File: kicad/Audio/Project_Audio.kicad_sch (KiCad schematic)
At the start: 9 parts, among them U1 PIC32MX170F256B, U2 Audio

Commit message: Revert to 3d98758
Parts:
- removed D1, D2: Diode, symbol ME218_BaseLib:Diode
- C1: value 10 uF -> Cap
- R1: value 100 k -> Res1
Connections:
- net GND: no longer C2.2, U1.8 (Vss)
- net at U1.14 (PGED3/5VT/RB5): now also U2. (Vol-)
- net at U1.15 (PGEC3/5VT/RB6): now also U2. (Vol-)
- net at U1.16 (5VT/RB7): now also U2. (Vol-)
- net at U1.18 (PGED2/5VT/RB9): now also U2. (Vol-)
- net at U1.21 (PGEC2/5VT/RB10): now also U2. (Vol-)
- net at U1.22 (RB11): now also U2. (Vol-)
- net at U1.23 (RB12): now also U2. (Vol-)
- net at U1.24 (RB13): now also U2. (Vol-)
- new net: C2.2, U1.8 (Vss)
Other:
- moved on the sheet: R1, U2

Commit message: Update audio kicad
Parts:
- added D? (x2): Diode, symbol ME218_BaseLib:Diode
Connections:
- net GND: now also C2.2, U1.8 (Vss)
- net PWN from main PIC32: now also D?.1 (K), D?.2 (A)
- net at C1.1, R1.2, U1.2 (RA0): now also D?.1 (K), D?.2 (A)
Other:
- moved on the sheet: R1
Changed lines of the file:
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@@
   (junction (at 69.85 85.09) (diameter 0) (color 0 0 0 0)
   )
+  (junction (at 63.5 85.09) (diameter 0) (color 0 0 0 0)
+  )
   (junction (at 85.09 111.76) (diameter 0) (color 0 0 0 0)
   )
@@
   (junction (at 151.13 127) (diameter 0) (color 0 0 0 0)
   )
+  (junction (at 44.45 85.09) (diameter 0) (color 0 0 0 0)
+  )
   (junction (at 85.09 104.14) (diameter 0) (color 0 0 0 0)
   )
@@
   (junction (at 85.09 67.31) (diameter 0) (color 0 0 0 0)
   )
+  (junction (at 85.09 74.93) (diameter 0) (color 0 0 0 0)
+  )
+  (wire (pts (xy 44.45 92.71) (xy 44.45 85.09))
+    (stroke (width 0) (type default) (color 0 0 0 0))
+  )
   (polyline (pts (xy 137.16 80.01) (xy 125.73 80.01))
     (stroke (width 0) (type default) (color 0 0 0 0))
@@
     (stroke (width 0) (type default) (color 0 0 0 0))
   )
-  (wire (pts (xy 55.88 85.09) (xy 58.42 85.09))
+  (wire (pts (xy 39.37 85.09) (xy 44.45 85.09))
     (stroke (width 0) (type default) (color 0 0 0 0))
   )
@@
     (stroke (width 0) (type default) (color 0 0 0 0))
   )
-  (wire (pts (xy 66.04 85.09) (xy 69.85 85.09))
+  (wire (pts (xy 57.15 85.09) (xy 63.5 85.09))
+    (stroke (width 0) (type default) (color 0 0 0 0))
+  )
+  (wire (pts (xy 63.5 85.09) (xy 69.85 85.09))
     (stroke (width 0) (type default) (color 0 0 0 0))
   )
@@
     (stroke (width 0) (type default) (color 0 0 0 0))
   )
+  (wire (pts (xy 49.53 92.71) (xy 44.45 92.71))
+    (stroke (width 0) (type default) (color 0 0 0 0))
+  )
   (wire (pts (xy 124.46 101.6) (xy 140.97 101.6))
     (stroke (width 0) (type default) (color 0 0 0 0))
   )
+  (wire (pts (xy 63.5 73.66) (xy 63.5 85.09))
+    (stroke (width 0) (type default) (color 0 0 0 0))
+  )
   (wire (pts (xy 124.46 91.44) (xy 140.97 91.44))
     (stroke (width 0) (type default) (color 0 0 0 0))
@@
     (stroke (width 0) (type default) (color 0 0 0 0))
   )
+  (wire (pts (xy 63.5 92.71) (xy 63.5 85.09))
+    (stroke (width 0) (type default) (color 0 0 0 0))
+  )
   (wire (pts (xy 124.46 78.74) (xy 129.54 78.74))
     (stroke (width 0) (type default) (color 0 0 0 0))
@@
     (stroke (width 0) (type default) (color 0 0 0 0))
   )
+  (wire (pts (xy 44.45 73.66) (xy 44.45 85.09))
+    (stroke (width 0) (type default) (color 0 0 0 0))
+  )
   (wire (pts (xy 168.91 83.82) (xy 168.91 127))
     (stroke (width 0) (type default) (color 0 0 0 0))
   )
+  (wire (pts (xy 57.15 92.71) (xy 63.5 92.71))
+    (stroke (width 0) (type default) (color 0 0 0 0))
+  )
   (wire (pts (xy 140.97 127) (xy 151.13 127))
     (stroke (width 0) (type default) (color 0 0 0 0))
@@
     (stroke (width 0) (type default) (color 0 0 0 0))
   )
+  (wire (pts (xy 57.15 73.66) (xy 63.5 73.66))
+    (stroke (width 0) (type default) (color 0 0 0 0))
+  )
   (wire (pts (xy 124.46 106.68) (xy 140.97 106.68))
     (stroke (width 0) (type default) (color 0 0 0 0))
   )
   (wire (pts (xy 160.02 114.3) (xy 160.02 127))
+    (stroke (width 0) (type default) (color 0 0 0 0))
+  )
+  (wire (pts (xy 49.53 73.66) (xy 44.45 73.66))
+    (stroke (width 0) (type default) (color 0 0 0 0))
+  )
+  (wire (pts (xy 44.45 85.09) (xy 49.53 85.09))
     (stroke (width 0) (type default) (color 0 0 0 0))
   )
@@
     (effects (font (size 1.27 1.27)) (justify left bottom))
   )
-  (global_label "PWN from main PIC32" (shape input) (at 55.88 85.09 180) (fields_autoplaced)
+  (global_label "PWN from main PIC32" (shape input) (at 39.37 85.09 180) (fields_autoplaced)
     (effects (font (size 1.27 1.27)) (justify right))
-    (property "Intersheet References" "${INTERSHEET_REFS}" (id 0) (at 31.9979 85.0106 0)
+    (property "Intersheet References" "${INTERSHEET_REFS}" (id 0) (at 15.4879 85.0106 0)
       (effects (font (size 1.27 1.27)) (justify right) hide)
     )
@@
     )
     (property "Datasheet" "" (id 3) (at 85.09 67.31 0)
+      (effects (font (size 1.27 1.27)) hide)
+    )
+    (pin "1")
+  )
+  (symbol (lib_id "power:GND") (at 85.09 74.93 0) (unit 1)
+    (in_bom yes) (on_board yes) (fields_autoplaced)
+    (property "Reference" "#PWR?" (id 0) (at 85.09 81.28 0)
+      (effects (font (size 1.27 1.27)) hide)
+    )
+    (property "Value" "GND" (id 1) (at 85.09 80.01 0))
+    (property "Footprint" "" (id 2) (at 85.09 74.93 0)
+      (effects (font (size 1.27 1.27)) hide)
+    )
+    (property "Datasheet" "" (id 3) (at 85.09 74.93 0)
       (effects (font (size 1.27 1.27)) hide)
     )
@@
     )
     (property "Datasheet" "" (id 3) (at 102.87 121.92 0)
+      (effects (font (size 1.27 1.27)) hide)
+    )
+    (pin "1")
+    (pin "2")
+  )
+  (symbol (lib_id "ME218_BaseLib:Diode") (at 53.34 73.66 180) (unit 1)
+    (in_bom yes) (on_board yes) (fields_autoplaced)
+    (property "Reference" "D?" (id 0) (at 53.34 67.31 0))
+    (property "Value" "Diode" (id 1) (at 53.34 69.85 0))
+    (property "Footprint" "" (id 2) (at 53.34 73.66 0)
+      (effects (font (size 1.27 1.27)) hide)
+    )
+    (property "Datasheet" "" (id 3) (at 53.34 73.66 0)
       (effects (font (size 1.27 1.27)) hide)
     )
@@
     (pin "2")
   )
-  (symbol (lib_id "ME218_BaseLib:Res1") (at 62.23 85.09 90) (unit 1)
-    (in_bom yes) (on_board yes) (fields_autoplaced)
-    (property "Reference" "R1" (id 0) (at 62.23 78.74 90))
-    (property "Value" "Res1" (id 1) (at 62.23 81.28 90))
-    (property "Footprint" "" (id 2) (at 62.484 84.074 90)
-      (effects (font (size 1.27 1.27)) hide)
-    )
-    (property "Datasheet" "" (id 3) (at 62.23 85.09 0)
+  (symbol (lib_id "ME218_BaseLib:Diode") (at 53.34 92.71 0) (unit 1)
+    (in_bom yes) (on_board yes)
+    (property "Reference" "D?" (id 0) (at 53.34 97.79 0))
+    (property "Value" "Diode" (id 1) (at 53.34 100.33 0))
+    (property "Footprint" "" (id 2) (at 53.34 92.71 0)
+      (effects (font (size 1.27 1.27)) hide)
+    )
+    (property "Datasheet" "" (id 3) (at 53.34 92.71 0)
+      (effects (font (size 1.27 1.27)) hide)
+    )
+    (pin "1")
+    (pin "2")
+  )
+  (symbol (lib_id "ME218_BaseLib:Res1") (at 53.34 85.09 90) (unit 1)
+    (in_bom yes) (on_board yes) (fields_autoplaced)
+    (property "Reference" "R1" (id 0) (at 53.34 78.74 90))
+    (property "Value" "Res1" (id 1) (at 53.34 81.28 90))
+    (property "Footprint" "" (id 2) (at 53.594 84.074 90)
+      (effects (font (size 1.27 1.27)) hide)
+    )
+    (property "Datasheet" "" (id 3) (at 53.34 85.09 0)
       (effects (font (size 1.27 1.27)) hide)
     )
@@
       (reference "#PWR08") (unit 1) (value "+5V") (footprint "")
     )
+    (path "/39f08828-7987-4a18-a65b-bd8b02efd613"
+      (reference "#PWR?") (unit 1) (value "GND") (footprint "")
+    )
     (path "/9936a45c-d9ed-4757-8965-fef1371db57d"
       (reference "C1") (unit 1) (value "Cap") (footprint "")
@@
       (reference "C4") (unit 1) (value "0.1 uF") (footprint "")
     )
+    (path "/919e989e-be09-45ed-a3b6-56c8307106d6"
+      (reference "D?") (unit 1) (value "Diode") (footprint "")
+    )
+    (path "/d73ebf58-e339-44ac-b350-416d66c9dcea"
+      (reference "D?") (unit 1) (value "Diode") (footprint "")
+    )
     (path "/df0418e5-cc6d-4e9d-b411-2c9742773b02"

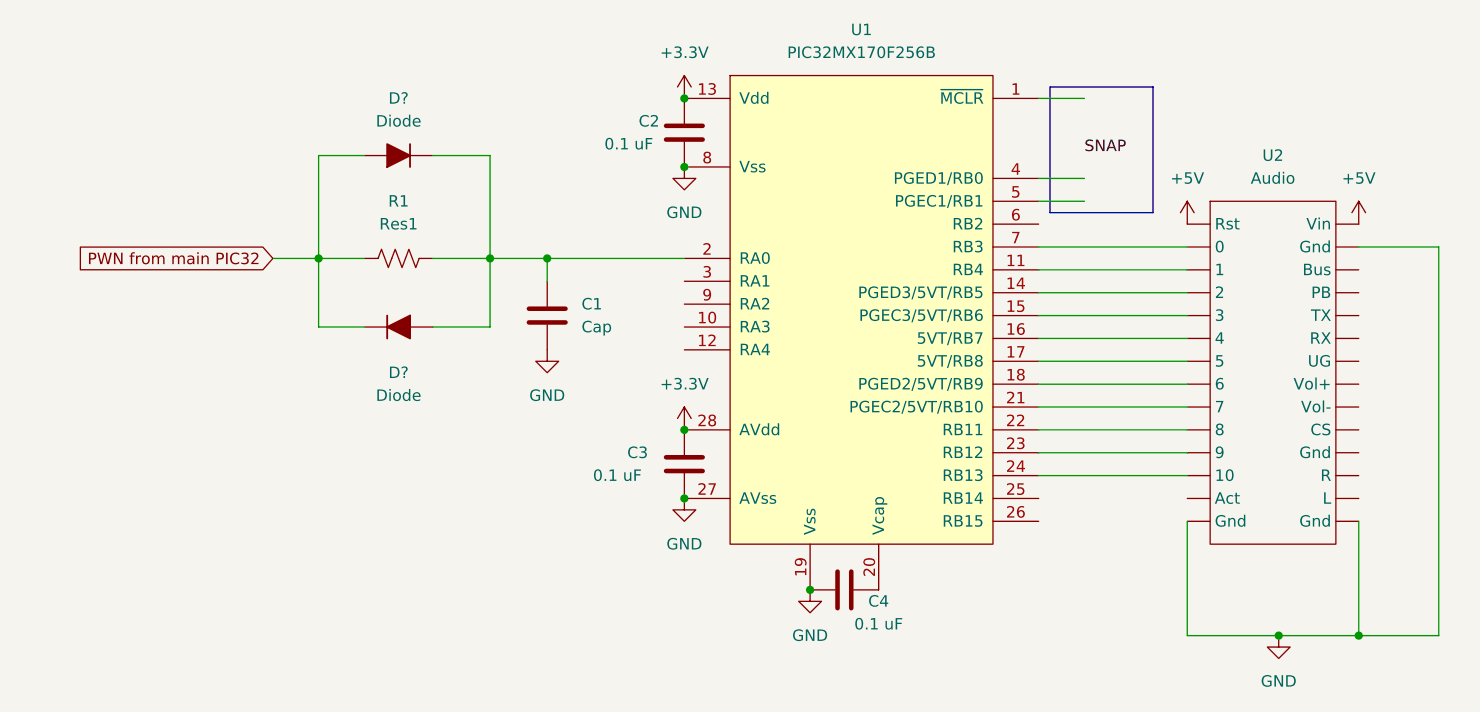
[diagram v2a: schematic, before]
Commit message: Add the values of resistance and capacitance in low pass filter.
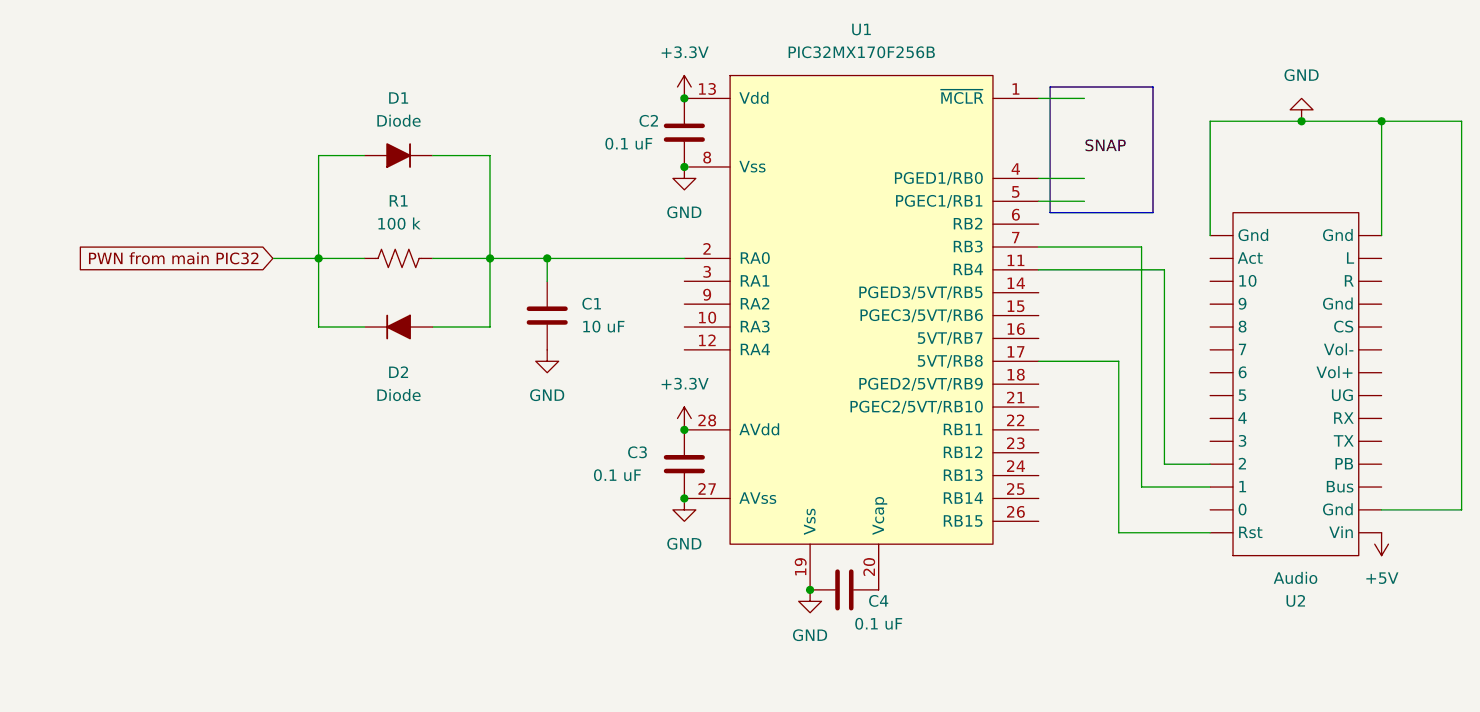
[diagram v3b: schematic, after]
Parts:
- C1: value Cap -> 10 uF
- R1: value Res1 -> 100 k
- gave numbers to parts that had none: 2
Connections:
- net at U1.14 (PGED3/5VT/RB5): no longer U2. (Vol-)
- net at U1.15 (PGEC3/5VT/RB6): no longer U2. (Vol-)
- net at U1.16 (5VT/RB7): no longer U2. (Vol-)
- net at U1.18 (PGED2/5VT/RB9): no longer U2. (Vol-)
- net at U1.21 (PGEC2/5VT/RB10): no longer U2. (Vol-)
- net at U1.22 (RB11): no longer U2. (Vol-)
- net at U1.23 (RB12): no longer U2. (Vol-)
- net at U1.24 (RB13): no longer U2. (Vol-)
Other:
- moved on the sheet: U2
